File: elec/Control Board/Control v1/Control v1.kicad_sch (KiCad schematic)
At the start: 68 parts, among them J1 DB9_Female_MountingHoles, J10 Conn_02x12_Odd_Even, J11 Screw_Terminal_01x02, J14 Conn_01x10, J2 Conn_01x08, J25 Screw_Terminal_01x02, J3 Conn_01x08, J4 Conn_01x08, J5 Conn_01x08, J6 Conn_01x08, J7 Conn_01x10, J8 Conn_02x18_Odd_Even, J9 Conn_01x10

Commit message: Lots of routing. Lots remaining.
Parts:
- removed TP103: Due_5V2, TestPoint:TestPoint_Loop_D2.54mm_Drill1.5mm_Beaded, symbol Connector:TestPoint
- added R301 (x2): 1R, Resistor_SMD:R_0603_1608Metric_Pad0.98x0.95mm_HandSolder, symbol Device:R
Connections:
- net 5V3 is gone; now on net +5V: J8.2 (Pin_2)
- net 5V4 is gone; now on net +5V: J8.1 (Pin_1)
- net +5V: now also A1.5V2 (SPI_5V)
- net D37: now also R301.2
- net D39: now also C301.1, J1.1
- net LOOPBACK13: now reaches A1.D36, J8.18 (Pin_18)
- net LOOPBACK13: now also R301.2
- net D38: now reaches A1.D38, J8.20 (Pin_20)
- net D38: now also R101.2
- net D40: now reaches A1.D40, J8.22 (Pin_22)
- net D42: now reaches A1.D42, J8.24 (Pin_24)
- net D44: now reaches A1.D44, J8.26 (Pin_26)
- net D46: now reaches A1.D46, J8.28 (Pin_28)
- net D48: now reaches A1.D48, J8.30 (Pin_30)
- net D50: now reaches A1.D50, J8.32 (Pin_32)
- net D53: now reaches A1.D53, J8.33 (Pin_33)
- net D52: now reaches A1.D52 (D52_CS2), J8.34 (Pin_34)
- removed net D35: C301.1, J1.1, R101.2
- new net Blower controller/LOOPBACK13: R301.1
- new net Blower controller/LOOPBACK25: R301.1
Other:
- sheet Blower controller ports: added LOOPBACK13, LOOPBACK25; removed none
- note added: "D38 and D39 for DB9 Loopback"
- moved on the sheet: R301

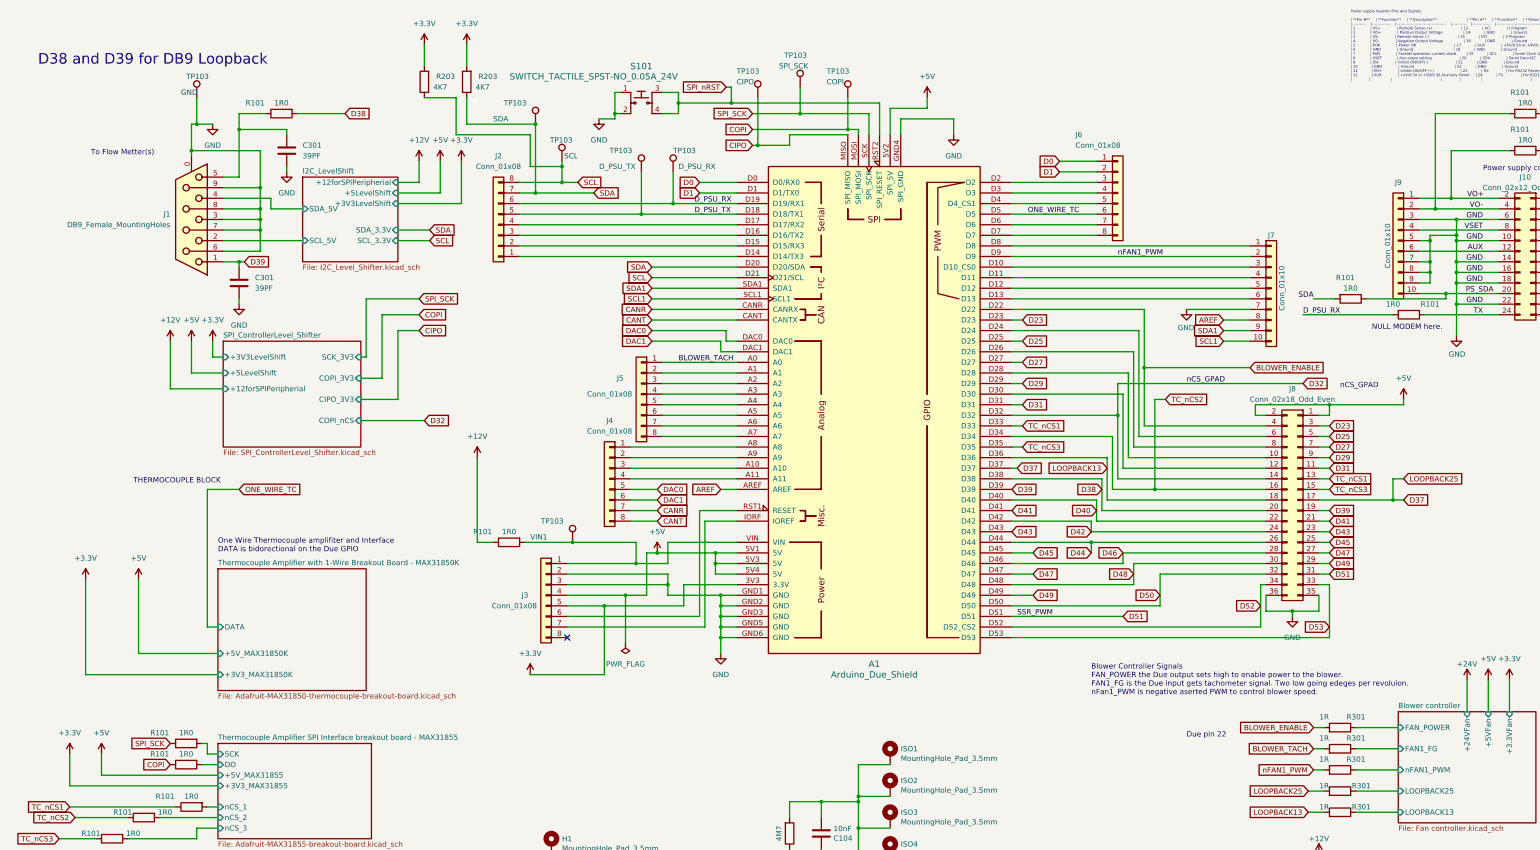
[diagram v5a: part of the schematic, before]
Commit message: Finishe routing on enlarged perimeter.
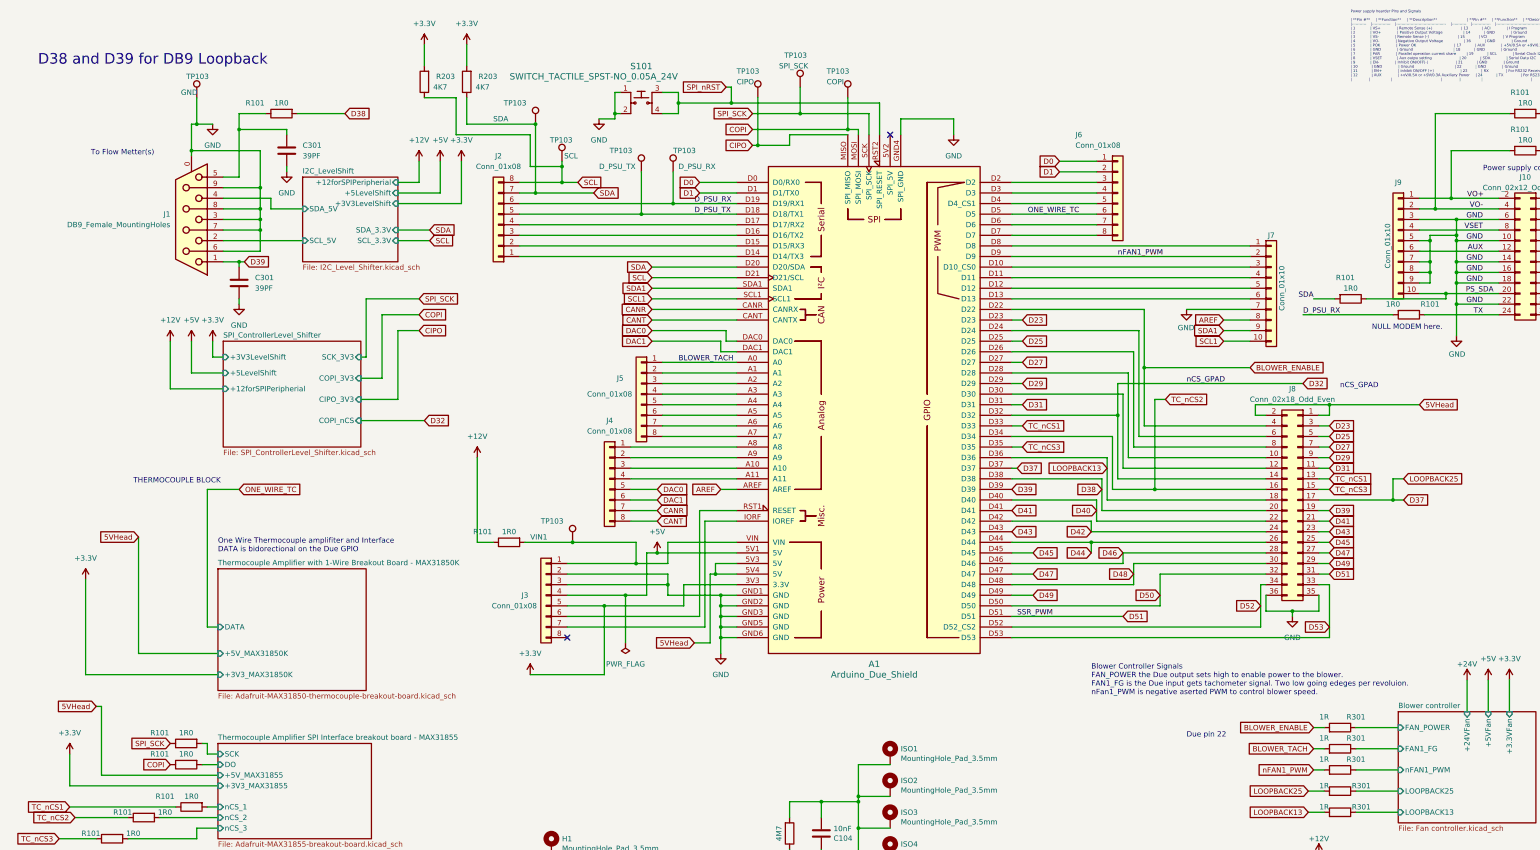
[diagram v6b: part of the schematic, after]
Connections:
- net +5V: no longer A1.5V2 (SPI_5V), A1.5V3 (5V), A1.5V4 (5V), J8.1 (Pin_1), J8.2 (Pin_2)
- new net 5VHead: A1.5V3 (5V), A1.5V4 (5V), J8.1 (Pin_1), J8.2 (Pin_2)
- no-connect marks 1 -> 2
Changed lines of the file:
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@@
   (junction (at 173.99 161.29) (diameter 0) (color 0 0 0 0)
   )
-  (junction (at 172.72 151.13) (diameter 0) (color 0 0 0 0)
-  )
   (junction (at 204.47 49.53) (diameter 0) (color 0 0 0 0)
   )
@@
   (junction (at 350.52 76.2) (diameter 0) (color 0 0 0 0)
   )
-  (junction (at 172.72 153.67) (diameter 0) (color 0 0 0 0)
-  )
   (junction (at 207.01 224.79) (diameter 0) (color 0 0 0 0)
   )
@@
   (junction (at 350.52 81.28) (diameter 0) (color 0 0 0 0)
   )
+  (junction (at 172.72 156.21) (diameter 0) (color 0 0 0 0)
+  )
   (junction (at 344.17 83.82) (diameter 0) (color 0 0 0 0)
   )
+  (no_connect (at 214.63 50.8))
   (no_connect (at 137.16 171.45))
   (wire (pts (xy 264.16 138.43) (xy 264.16 143.51))
@@
     (stroke (width 0) (type default))
   )
+  (wire (pts (xy 171.45 156.21) (xy 172.72 156.21))
+    (stroke (width 0) (type default))
+  )
   (wire (pts (xy 96.52 76.2) (xy 104.14 76.2))
     (stroke (width 0) (type default))
@@
     (stroke (width 0) (type default))
   )
+  (wire (pts (xy 167.64 172.72) (xy 171.45 172.72))
+    (stroke (width 0) (type default))
+  )
   (wire (pts (xy 419.1 93.98) (xy 402.59 93.98))
     (stroke (width 0) (type default))
@@
     (stroke (width 0) (type default))
   )
-  (wire (pts (xy 223.52 41.91) (xy 223.52 44.45))
-    (stroke (width 0) (type default))
-  )
   (wire (pts (xy 304.8 161.29) (xy 304.8 165.1))
     (stroke (width 0) (type default))
@@
     (stroke (width 0) (type default))
   )
-  (wire (pts (xy 214.63 44.45) (xy 223.52 44.45))
-    (stroke (width 0) (type default))
-  )
   (wire (pts (xy 353.06 181.61) (xy 353.06 189.23))
     (stroke (width 0) (type default))
@@
     (stroke (width 0) (type default))
   )
-  (wire (pts (xy 214.63 44.45) (xy 214.63 50.8))
-    (stroke (width 0) (type default))
-  )
   (wire (pts (xy 182.88 53.34) (xy 190.5 53.34))
     (stroke (width 0) (type default))
@@
     (stroke (width 0) (type default))
   )
-  (wire (pts (xy 337.82 115.57) (xy 337.82 114.3))
-    (stroke (width 0) (type default))
-  )
   (wire (pts (xy 53.34 175.26) (xy 34.29 175.26))
     (stroke (width 0) (type default))
@@
     (stroke (width 0) (type default))
   )
+  (wire (pts (xy 171.45 172.72) (xy 171.45 156.21))
+    (stroke (width 0) (type default))
+  )
+  (wire (pts (xy 25.4 187.96) (xy 24.13 187.96))
+    (stroke (width 0) (type default))
+  )
   (wire (pts (xy 54.61 68.58) (xy 63.5 68.58))
     (stroke (width 0) (type default))
@@
     (stroke (width 0) (type default))
   )
-  (wire (pts (xy 172.72 151.13) (xy 172.72 153.67))
-    (stroke (width 0) (type default))
-  )
   (wire (pts (xy 335.28 133.35) (xy 335.28 138.43))
     (stroke (width 0) (type default))
@@
     (stroke (width 0) (type default))
   )
-  (wire (pts (xy 172.72 151.13) (xy 177.8 151.13))
-    (stroke (width 0) (type default))
-  )
   (wire (pts (xy 152.4 140.97) (xy 158.75 140.97))
     (stroke (width 0) (type default))
@@
     (stroke (width 0) (type default))
   )
-  (wire (pts (xy 34.29 175.26) (xy 34.29 157.48))
+  (wire (pts (xy 34.29 147.32) (xy 34.29 175.26))
     (stroke (width 0) (type default))
   )
@@
     (stroke (width 0) (type default))
   )
-  (wire (pts (xy 320.04 115.57) (xy 337.82 115.57))
+  (wire (pts (xy 320.04 115.57) (xy 341.63 115.57))
     (stroke (width 0) (type default))
   )
@@
     (stroke (width 0) (type default))
   )
-  (wire (pts (xy 25.4 204.47) (xy 25.4 199.39))
+  (wire (pts (xy 25.4 187.96) (xy 25.4 204.47))
     (stroke (width 0) (type default))
   )
@@
     (stroke (width 0) (type default))
   )
-  (wire (pts (xy 158.75 151.13) (xy 172.72 151.13))
+  (wire (pts (xy 158.75 151.13) (xy 177.8 151.13))
     (stroke (width 0) (type default))
   )
@@
     )
   )
+  (global_label "5VHead" (shape input) (at 167.64 172.72 180) (fields_autoplaced)
+    (effects (font (size 1.27 1.27)) (justify right))
+    (property "Intersheetrefs" "${INTERSHEET_REFS}" (at 157.719 172.72 0)
+      (effects (font (size 1.27 1.27)) (justify right) hide)
+    )
+  )
   (global_label "TC_nCS3" (shape input) (at 15.24 219.71 180) (fields_autoplaced)
     (effects (font (size 1.27 1.27)) (justify right))
@@
     )
   )
+  (global_label "5VHead" (shape input) (at 34.29 147.32 180) (fields_autoplaced)
+    (effects (font (size 1.27 1.27)) (justify right))
+    (property "Intersheetrefs" "${INTERSHEET_REFS}" (at 24.369 147.32 0)
+      (effects (font (size 1.27 1.27)) (justify right) hide)
+    )
+  )
   (global_label "BLOWER_TACH" (shape input) (at 316.23 198.12 180) (fields_autoplaced)
     (effects (font (size 1.27 1.27)) (justify right))
@@
     )
   )
+  (global_label "5VHead" (shape input) (at 341.63 115.57 0) (fields_autoplaced)
+    (effects (font (size 1.27 1.27)) (justify left))
+    (property "Intersheetrefs" "${INTERSHEET_REFS}" (at 351.551 115.57 0)
+      (effects (font (size 1.27 1.27)) (justify left) hide)
+    )
+  )
   (global_label "LOOPBACK13" (shape input) (at 266.7 130.81 180) (fields_autoplaced)
     (effects (font (size 1.27 1.27)) (justify right))
@@
     )
   )
+  (global_label "5VHead" (shape input) (at 24.13 187.96 180) (fields_autoplaced)
+    (effects (font (size 1.27 1.27)) (justify right))
+    (property "Intersheetrefs" "${INTERSHEET_REFS}" (at 14.209 187.96 0)
+      (effects (font (size 1.27 1.27)) (justify right) hide)
+    )
+  )
   (global_label "D38" (shape input) (at 265.43 135.89 180) (fields_autoplaced)
     (effects (font (size 1.27 1.27)) (justify right))
@@
     )
   )
-  (symbol (lib_id "power:+5V") (at 34.29 157.48 0) (unit 1)
-    (in_bom yes) (on_board yes) (dnp no) (fields_autoplaced)
-    (property "Reference" "#PWR02" (at 34.29 161.29 0)
-      (effects (font (size 1.27 1.27)) hide)
-    )
-    (property "Value" "+5V" (at 34.29 152.4 0)
-      (effects (font (size 1.27 1.27)))
-    )
-    (property "Footprint" "" (at 34.29 157.48 0)
-      (effects (font (size 1.27 1.27)) hide)
-    )
-    (property "Datasheet" "" (at 34.29 157.48 0)
-      (effects (font (size 1.27 1.27)) hide)
-    )
-    (pin "1")
-    (instances
-      (project "Control v1"
-        (path "/c68c9deb-8d4d-42f0-adf8-4d3022f4ee59"
-          (reference "#PWR02") (unit 1)
-        )
-      )
-    )
-  )
   (symbol (lib_id "power:+24V") (at 353.06 181.61 0) (unit 1)
     (in_bom yes) (on_board yes) (dnp no) (fields_autoplaced)
@@
     )
   )
-  (symbol (lib_id "power:+5V") (at 337.82 114.3 0) (unit 1)
-    (in_bom yes) (on_board yes) (dnp no) (fields_autoplaced)
-    (property "Reference" "#PWR080" (at 337.82 118.11 0)
-      (effects (font (size 1.27 1.27)) hide)
-    )
-    (property "Value" "+5V" (at 337.82 109.22 0)
-      (effects (font (size 1.27 1.27)))
-    )
-    (property "Footprint" "" (at 337.82 114.3 0)
-      (effects (font (size 1.27 1.27)) hide)
-    )
-    (property "Datasheet" "" (at 337.82 114.3 0)
-      (effects (font (size 1.27 1.27)) hide)
-    )
-    (pin "1")
-    (instances
-      (project "Control v1"
-        (path "/c68c9deb-8d4d-42f0-adf8-4d3022f4ee59"
-          (reference "#PWR080") (unit 1)
-        )
-      )
-    )
-  )
   (symbol (lib_id "power:+12V") (at 115.57 128.27 0) (unit 1)
     (in_bom yes) (on_board yes) (dnp no) (fields_autoplaced)
@@
     )
   )
-  (symbol (lib_id "power:+5V") (at 223.52 41.91 0) (unit 1)
-    (in_bom yes) (on_board yes) (dnp no) (fields_autoplaced)
-    (property "Reference" "#PWR081" (at 223.52 45.72 0)
-      (effects (font (size 1.27 1.27)) hide)
-    )
-    (property "Value" "+5V" (at 223.52 36.83 0)
-      (effects (font (size 1.27 1.27)))
-    )
-    (property "Footprint" "" (at 223.52 41.91 0)
-      (effects (font (size 1.27 1.27)) hide)
-    )
-    (property "Datasheet" "" (at 223.52 41.91 0)
-      (effects (font (size 1.27 1.27)) hide)
-    )
-    (pin "1")
-    (instances
-      (project "Control v1"
-        (path "/c68c9deb-8d4d-42f0-adf8-4d3022f4ee59"
-          (reference "#PWR081") (unit 1)
-        )
-      )
-    )
-  )
   (symbol (lib_id "Device:R") (at 68.58 45.72 90) (mirror x) (unit 1)
     (in_bom yes) (on_board yes) (dnp no)
@@
         )
       )
-    )
-  )
-  (symbol (lib_id "power:+5V") (at 25.4 199.39 0) (unit 1)
-    (in_bom yes) (on_board yes) (dnp no) (fields_autoplaced)
-    (property "Reference" "#PWR01" (at 25.4 203.2 0)
-      (effects (font (size 1.27 1.27)) hide)
-    )
-    (property "Value" "+5V" (at 25.4 194.31 0)
-      (effects (font (size 1.27 1.27)))
-    )
-    (property "Footprint" "" (at 25.4 199.39 0)
-      (effects (font (size 1.27 1.27)) hide)
-    )
-    (property "Datasheet" "" (at 25.4 199.39 0)
-      (effects (font (size 1.27 1.27)) hide)
-    )
-    (pin "1")
-    (instances
-      (project "Control v1"
-        (path "/c68c9deb-8d4d-42f0-adf8-4d3022f4ee59"
-          (reference "#PWR01") (unit 1)
-        )
-      )
